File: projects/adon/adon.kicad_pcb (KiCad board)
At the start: 2 copper layers, 55.9 x 30.5 mm, 31 parts, among them IC1 STM32F030F4, P1 BATTERY, P2 SWD, Q1 2N3704, SW1 POWER, SW2 BUTTON0, SW3 BUTTON1, SW4 BUTTON2, SW5 BUTTON3

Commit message: done
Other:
- board text added: "Adon v5 arolsen@gmail.com"
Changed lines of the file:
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@@
     (links 65)
     (no_connects 0)
-    (area 13.157999 13.157999 69.138001 43.738001)
+    (area 11.27881 10.49274 70.539126 43.815001)
     (thickness 1.6)
-    (drawings 4)
+    (drawings 5)
     (tracks 266)
     (zones 0)
@@
     (visible_elements FFFFFF7F)
     (pcbplotparams
-      (layerselection 3178497)
+      (layerselection 284196865)
       (usegerberextensions true)
       (excludeedgelayer true)
@@
       (outputformat 1)
       (mirror false)
-      (drillshape 1)
+      (drillshape 0)
       (scaleselection 1)
-      (outputdirectory ""))
+      (outputdirectory /home/storage/Projects/kicad/projects/adon/gerber/))
   )
   (net 0 "")
@@
     )
   )
+  (gr_text "Adon v5\narolsen@gmail.com" (at 62.6872 18.7579) (layer B.SilkS)
+    (effects (font (size 2 1.5) (thickness 0.3)) (justify left mirror))
+  )
   (gr_line (start 69.088 13.208) (end 13.208 13.208) (angle 90) (layer Edge.Cuts) (width 0.1))

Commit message: better
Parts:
- D1: value ERROR -> FAIL!
- moved R4 26.9 mm to (66.8, 38.6), turned to 270 degrees
- moved D1 25.1 mm to (54.6, 15.2)
- moved R5 25.1 mm to (41.4, 30.5)
- moved R7 13.6 mm to (27.9, 30.5)
- moved R6 13.3 mm to (15.5, 32.0), turned to 90 degrees
- moved R2 13.2 mm to (59.7, 15.2), turned to 0 degrees
- moved SP1 13.1 mm to (28.2, 23.6), turned to 0 degrees
- moved JP1 12.9 mm to (45.2, 15.2)
- moved D6 12.8 mm to (32.0, 15.2)
- moved R9 12.2 mm to (41.4, 26.7)
- moved R1 11.0 mm to (35.1, 22.1), turned to 180 degrees
- moved Q1 4.88 mm to (37.6, 16.3), turned to 90 degrees
- moved C1 1.19 mm to (24.9, 16.3), turned to 180 degrees
- moved IC1 1.05 mm to (53.6, 21.3)
- moved C4 0.90 mm to (47.2, 21.1), turned to 90 degrees
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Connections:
- D2 pad 2: GND -> Net-(D2-Pad2)
- D3 pad 2: GND -> Net-(D3-Pad2)
- D4 pad 2: GND -> Net-(D4-Pad2)
- D5 pad 2: GND -> Net-(D5-Pad2)
- IC1 pad 14: Net-(D1-Pad1) -> Net-(IC1-Pad14)
- IC1 pad 17: Net-(IC1-Pad17) -> Net-(D1-Pad1)
- IC1 pad 6: Net-(IC1-Pad6) -> Net-(D5-Pad1)
- IC1 pad 7: Net-(IC1-Pad7) -> Net-(D4-Pad1)
- IC1 pad 8: Net-(IC1-Pad8) -> Net-(D3-Pad1)
- IC1 pad 9: Net-(IC1-Pad9) -> Net-(D2-Pad1)
- R3 pad 1: Net-(IC1-Pad9) -> Net-(D2-Pad2)
- R3 pad 2: Net-(D2-Pad1) -> GND
- R4 pad 1: Net-(IC1-Pad8) -> Net-(D3-Pad2)
- R4 pad 2: Net-(D3-Pad1) -> GND
- R5 pad 1: Net-(IC1-Pad7) -> Net-(D4-Pad2)
- R5 pad 2: Net-(D4-Pad1) -> GND
- R6 pad 1: Net-(IC1-Pad6) -> Net-(D5-Pad2)
- R6 pad 2: Net-(D5-Pad1) -> GND
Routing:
- net GND: track 87.3 -> 35.8 mm, vias 5 -> 11
- net Net-(D5-Pad1): track 7.20 -> 38.3 mm, vias 0 -> 1
- net Net-(D6-Pad2): track 2.52 -> 32.7 mm
- net Net-(D1-Pad2): track 2.56 -> 30.4 mm
- net Net-(IC1-Pad6): track 25.5 -> 0.00 mm, vias 2 -> 0
- net Net-(D1-Pad1): track 30.9 -> 6.49 mm
- net Net-(D3-Pad2): track 0.00 -> 22.1 mm
- net Net-(IC1-Pad1): track 32.6 -> 16.5 mm
- net Net-(IC1-Pad8): track 15.7 -> 0.00 mm
- net Net-(IC1-Pad7): track 14.5 -> 0.00 mm, vias 2 -> 0
- net VDD: track 179.4 -> 193.0 mm
- net SWDIO: track 25.6 -> 12.0 mm
- net Net-(D4-Pad1): track 33.0 -> 20.6 mm, vias 1 -> 0
- net NRST: track 21.8 -> 32.5 mm
- net Net-(D2-Pad2): track 0.00 -> 10.5 mm
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- added copper zone on F.Cu, net VDD
- removed copper zone on F.Cu, net GND

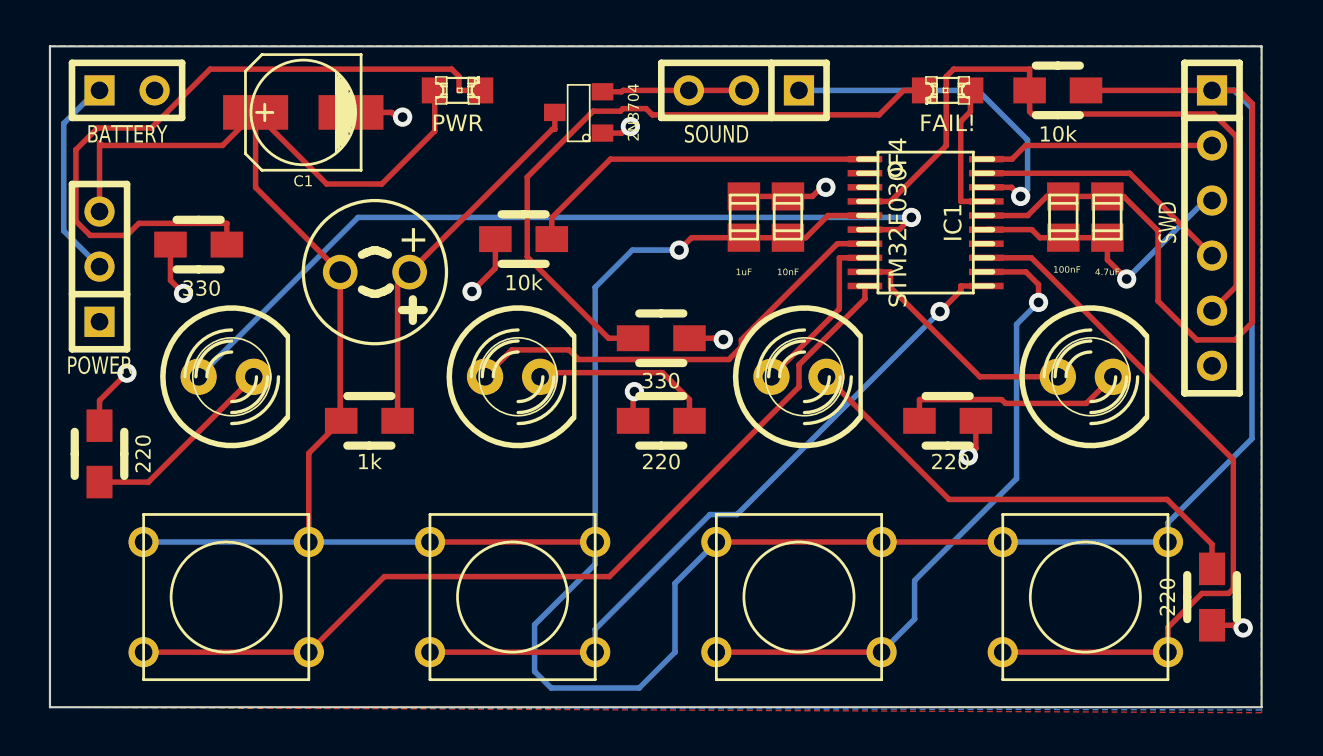
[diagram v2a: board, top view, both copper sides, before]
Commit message: add tag-connect libraries, redo adon board
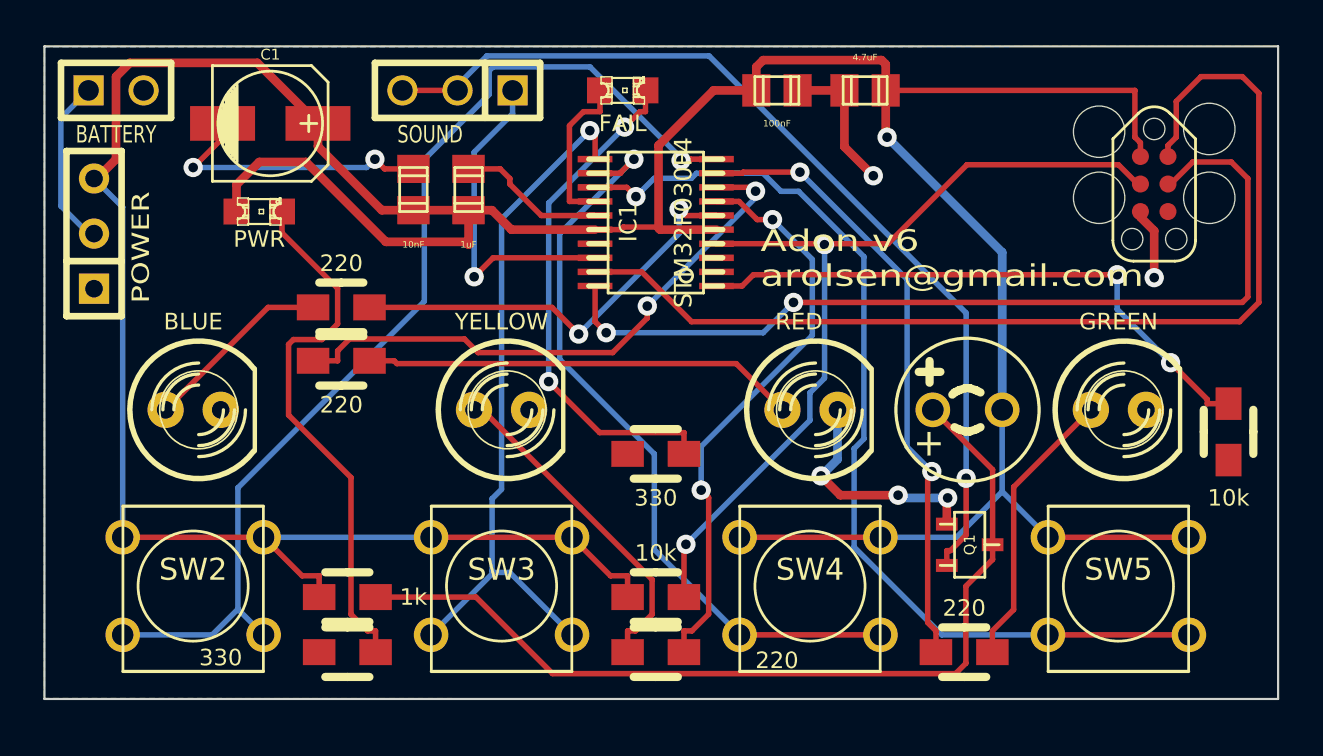
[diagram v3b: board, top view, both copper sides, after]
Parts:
- D1: value FAIL! -> PWR
- D2: value LED3 -> GREEN
- D3: value LED2 -> RED
- D4: value LED1 -> YELLOW
- D5: value LED0 -> BLUE
- D6: value PWR -> FAIL
- JP1: footprint Connect:SIL-3 -> synic:SIL-3
- P1: footprint Connect:SIL-2 -> synic:SIL-2
- P2: value SWD -> TC2030-CTX; footprint Connect:SIL-6 -> Tag-Connect:TC2030_SMALL
- Q1: value 2N3704 -> NPN; footprint SMD_Packages:SOT23 -> synic:sot23transistor
- R1, R2, R4, R5, R6, R9: footprint Resistors_SMD:Resistor_SMD0805_HandSoldering_RevA_Date21Jun2010 -> Resistors_SMD:Resistor_SMD0805_HandSoldering
- R3: value 220 -> 330; footprint Resistors_SMD:Resistor_SMD0805_HandSoldering_RevA_Date21Jun2010 -> Resistors_SMD:Resistor_SMD0805_HandSoldering
- R7: value 1k -> 220; footprint Resistors_SMD:Resistor_SMD0805_HandSoldering_RevA_Date21Jun2010 -> Resistors_SMD:Resistor_SMD0805_HandSoldering
- R8: value 330 -> 1k; footprint Resistors_SMD:Resistor_SMD0805_HandSoldering_RevA_Date21Jun2010 -> Resistors_SMD:Resistor_SMD0805_HandSoldering
- SW2, SW3, SW4, SW5: footprint Discret:SW_PUSH_SMALL -> synic:SW_PUSH_SMALL
- moved R1 33.7 mm to (67.6, 31.0), turned to 270 degrees
- moved D1 32.2 mm to (22.9, 20.8), turned to 0 degrees
- moved R2 29.8 mm to (41.1, 38.6), turned to 180 degrees
- moved R3 29.7 mm to (26.9, 41.1), turned to 180 degrees
- moved SP1 28.1 mm to (55.5, 30.0), turned to 180 degrees
- moved R6 27.2 mm to (41.1, 41.1), turned to 180 degrees
- moved Q1 26.9 mm to (55.6, 36.2), turned to 270 degrees
- moved R8 17.6 mm to (26.9, 38.6), turned to 0 degrees
- moved C4 17.3 mm to (30.0, 19.8)
- moved R5 15.0 mm to (26.6, 27.7), turned to 0 degrees
- moved C5 14.4 mm to (46.7, 15.2), turned to 0 degrees
- moved JP1 13.2 mm to (32.0, 15.2)
- moved C2 12.8 mm to (32.5, 19.8)
- moved C3 12.6 mm to (50.8, 15.2), turned to 180 degrees
- moved IC1 12.4 mm to (41.1, 21.3), turned to 90 degrees
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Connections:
- D1 pad 1: Net-(D1-Pad1) -> VDD
- D2 pad 2: Net-(D2-Pad2) -> GND
- D3 pad 2: Net-(D3-Pad2) -> GND
- D4 pad 2: Net-(D4-Pad2) -> GND
- D5 pad 2: Net-(D5-Pad2) -> GND
- D6 pad 1: VDD -> Net-(D6-Pad1)
- IC1 pad 14: Net-(IC1-Pad14) -> Net-(D6-Pad1)
- IC1 pad 17: Net-(D1-Pad1) -> Net-(IC1-Pad17)
- IC1 pad 6: Net-(D5-Pad1) -> Net-(IC1-Pad6)
- IC1 pad 7: Net-(D4-Pad1) -> Net-(IC1-Pad7)
- IC1 pad 8: Net-(D3-Pad1) -> Net-(IC1-Pad8)
- IC1 pad 9: Net-(D2-Pad1) -> Net-(IC1-Pad9)
- P2 pad 2: SWCLK -> SWDIO
- P2 pad 3: GND -> NRST
- P2 pad 4: SWDIO -> SWCLK
- P2 pad 5: NRST -> GND
- R3 pad 1: Net-(D2-Pad2) -> Net-(D1-Pad2)
- R4 pad 1: Net-(D3-Pad2) -> Net-(IC1-Pad9)
- R4 pad 2: GND -> Net-(D2-Pad1)
- R5 pad 1: Net-(D4-Pad2) -> Net-(IC1-Pad8)
- R5 pad 2: GND -> Net-(D3-Pad1)
- R6 pad 1: Net-(D5-Pad2) -> Net-(IC1-Pad7)
- R6 pad 2: GND -> Net-(D4-Pad1)
- R7 pad 1: VDD -> Net-(IC1-Pad6)
- R7 pad 2: Net-(Q1-Pad3) -> Net-(D5-Pad1)
- R8 pad 1: Net-(D6-Pad2) -> VDD
- R8 pad 2: GND -> Net-(Q1-Pad3)
- R9 pad 1: Net-(D1-Pad2) -> Net-(D6-Pad2)
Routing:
- net Net-(JP1-Pad2): track 6.55 -> 43.8 mm, vias 0 -> 1
- net SWDIO: track 12.0 -> 48.9 mm
- net SWCLK: track 10.7 -> 42.5 mm, vias 0 -> 2
- net Net-(D5-Pad1): track 38.3 -> 8.76 mm, vias 1 -> 0
- net Net-(IC1-Pad9): track 0.00 -> 28.8 mm, vias 0 -> 2
- net Net-(IC1-Pad8): track 0.00 -> 26.8 mm, vias 0 -> 2
- net Net-(IC1-Pad7): track 0.00 -> 26.6 mm, vias 0 -> 2
- net Net-(Q1-Pad3): track 17.3 -> 42.2 mm
- net Net-(D3-Pad2): track 22.1 -> 0.00 mm
- net Net-(IC1-Pad6): track 0.00 -> 19.7 mm, vias 0 -> 2
- net VDD: track 193.0 -> 174.6 mm
- net Net-(D3-Pad1): track 7.97 -> 20.0 mm
- net Net-(IC1-Pad13): track 33.7 -> 45.3 mm, vias 0 -> 1
- net Net-(IC1-Pad1): track 16.5 -> 27.3 mm, vias 0 -> 2
- net Net-(D2-Pad2): track 10.5 -> 0.00 mm
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- added copper zone on F.Cu, net GND
- removed copper zone on F.Cu, net VDD
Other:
- board size 55.9 x 30.5 mm -> 56.9 x 30.1 mm
- net class TAG-CONNECT added: clearance 0.125, trace_width 0.254, via_dia 0.889, via_drill 0.635
- net class VCC added: clearance 0.254, trace_width 0.4, via_dia 0.889, via_drill 0.635
- board text added: "Adon v6 arolsen@gmail.com"
- board text removed: "Adon v5 arolsen@gmail.com"

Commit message: stuff
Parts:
- removed P2: TC2030-CTX, Tag-Connect:TC2030_SMALL
- added C6: 10uF, Capacitors_SMD:c_elec_4x4.5, F.Cu at (24.1, 23.4)
- added P3: SWD, synic:SIL-5, F.Cu at (67.6, 21.6)
- D2: value GREEN -> LED3
- D3: value RED -> LED2
- D4: value YELLOW -> LED1
- D5: value BLUE -> LED0
- Q1: value NPN -> NPN2
- moved R7 29.6 mm to (55.4, 32.3)
- moved R5 28.8 mm to (55.4, 29.8)
- moved R9 26.3 mm to (15.0, 29.1), turned to 270 degrees
- moved D1 18.4 mm to (40.4, 15.1), turned to 180 degrees
- moved R6 16.4 mm to (26.9, 33.0)
- moved Q1 15.4 mm to (41.3, 30.7), turned to 180 degrees
- moved R4 14.8 mm to (67.7, 32.9), turned to 90 degrees
- moved R1 14.4 mm to (55.4, 38.7), turned to 0 degrees
- moved SP1 13.2 mm to (59.7, 17.4)
- moved R3 10.7 mm to (26.9, 30.5)
- moved C5 5.11 mm to (48.0, 20.2), turned to 270 degrees
- moved D6 5.08 mm to (44.7, 15.1)
- moved C3 4.98 mm to (50.3, 20.2), turned to 270 degrees
- moved C2 2.82 mm to (29.7, 20.2)
- moved C4 2.07 mm to (32.0, 20.2)
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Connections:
- JP1 pad 1: Net-(IC1-Pad18) -> Net-(IC1-Pad13)
- Q1 pad 1: GND -> Net-(JP1-Pad2)
- Q1 pad 2: Net-(JP1-Pad2) -> GND
- SW5 pad 2: Net-(IC1-Pad13) -> Net-(IC1-Pad18)
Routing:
- net Net-(D5-Pad1): track 8.76 -> 48.5 mm, vias 0 -> 1
- net NRST: track 40.4 -> 72.8 mm, vias 2 -> 0
- net Net-(IC1-Pad12): track 35.4 -> 66.6 mm, vias 1 -> 0
- net Net-(IC1-Pad13): track 45.3 -> 16.7 mm, vias 1 -> 0
- net Net-(IC1-Pad18): track 15.3 -> 43.1 mm
- net Net-(JP1-Pad2): track 43.8 -> 21.6 mm
- net SWDIO: track 48.9 -> 27.7 mm
- net Net-(D6-Pad2): track 23.6 -> 44.5 mm, vias 2 -> 0
- net Net-(IC1-Pad10): track 49.5 -> 30.3 mm, vias 1 -> 0
- net SWCLK: track 42.5 -> 26.9 mm, vias 2 -> 0
- net GND: track 40.8 -> 56.3 mm
- net VDD: track 174.6 -> 188.2 mm, vias 1 -> 2
- net Net-(IC1-Pad7): track 26.6 -> 14.9 mm, vias 2 -> 0
- net Net-(Q1-Pad3): track 42.2 -> 52.4 mm, vias 0 -> 1
- net Net-(D3-Pad1): track 20.0 -> 11.3 mm
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
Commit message: totally updated, gonna be awesome
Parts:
- JP1: footprint synic:SIL-3 -> Pin_Headers:Pin_Header_Straight_1x03
- P1: footprint synic:SIL-2 -> jst-2-pth-ra
- P3: footprint synic:SIL-5 -> Pin_Headers:Pin_Header_Angled_1x05
- R9: value 330 -> 220
- moved R9 36.0 mm to (48.3, 15.2), turned to 0 degrees
- moved R1 14.5 mm to (41.1, 36.1)
- moved R4 13.6 mm to (55.4, 38.6), turned to 0 degrees
- moved P3 8.27 mm to (59.4, 20.1)
- moved C1 6.34 mm to (20.6, 22.4)
- moved C6 5.46 mm to (25.8, 18.2), turned to 270 degrees
- moved P1 5.18 mm to (21.3, 16.3), turned to 90 degrees
- moved SP1 5.12 mm to (54.6, 16.8), turned to 270 degrees
- moved SW1 4.07 mm to (15.0, 25.9)
- moved D1 1.53 mm to (38.9, 15.2)
- moved D6 1.28 mm to (43.4, 15.2)
- moved SW2 0.51 mm to (19.8, 38.6)
- moved SW3 0.51 mm to (34.0, 38.6)
- moved SW4 0.51 mm to (48.3, 38.6)
- moved SW5 0.51 mm to (62.5, 38.6)
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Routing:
- net GND: track 56.3 -> 128.7 mm, vias 7 -> 9
- net Net-(Q1-Pad3): track 52.4 -> 95.2 mm, vias 1 -> 0
- net Net-(D6-Pad2): track 44.5 -> 2.48 mm
- net Net-(IC1-Pad12): track 66.6 -> 30.5 mm, vias 0 -> 1
- net VDD: track 188.2 -> 161.6 mm, vias 2 -> 0
- net Net-(D1-Pad2): track 20.6 -> 46.7 mm, vias 2 -> 0
- net Net-(IC1-Pad9): track 35.4 -> 24.1 mm
- net Net-(D5-Pad1): track 48.5 -> 38.0 mm
- net Net-(IC1-Pad1): track 29.6 -> 19.1 mm
- net SWDIO: track 27.7 -> 18.7 mm, vias 0 -> 1
- net Net-(IC1-Pad18): track 43.1 -> 35.3 mm
- net Net-(P1-Pad1): track 8.29 -> 15.8 mm
- net Net-(IC1-Pad13): track 16.7 -> 22.7 mm
- net SWCLK: track 26.9 -> 21.2 mm
- net Net-(IC1-Pad11): track 27.7 -> 32.9 mm
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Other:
- board text added: "Adon v7"
- board text added: "Adon v7 arolsen@gmail.com"
- board text added: "arolsen@gmail.com"
- board text removed: "Adon v6 arolsen@gmail.com"
